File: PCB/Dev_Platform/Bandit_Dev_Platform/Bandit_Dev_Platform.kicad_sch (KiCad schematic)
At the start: 112 parts, among them J1 Conn_01x03_Pin, J10 Conn_01x05_Pin, J11 Conn_01x05_Pin, J2 SMA, J3 Conn_01x05_Pin, J4 Conn_01x05_Pin, J5 BNC, J6 BNC, J7 SMA, J8 Conn_01x05_Pin, J9 Conn_01x06_Pin, P1 USB_C_Plug_USB2.0, SW1 SW_SPST, U1 AD7253, U1 OPA1664, U2 RP2040, U3 AP2210N-4.0TRG1, U4 NCP164ASNADJT1G, U5 W25Q32JVSS, U6 MCP6486UT-E/OT, U7 MCP6S92-E/SN, Y1 12MHz

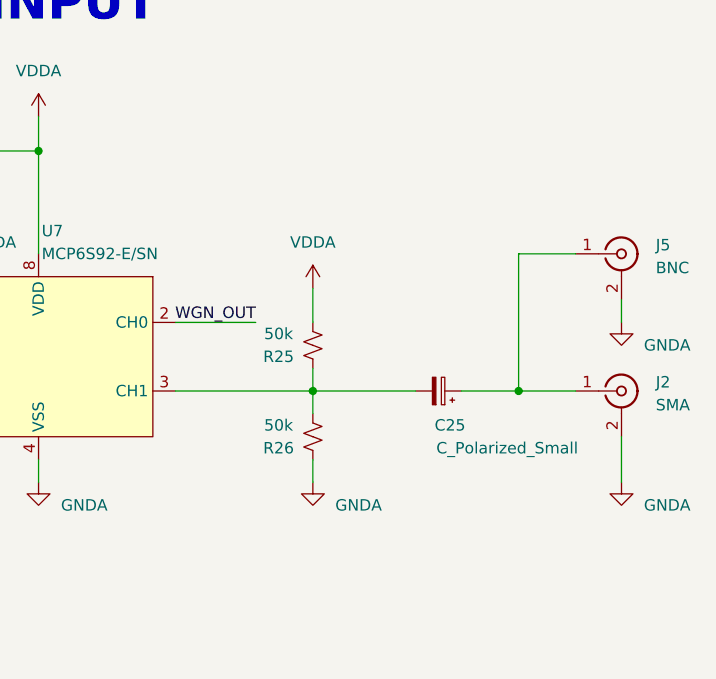
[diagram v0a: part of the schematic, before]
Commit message: update pcb, filter kinda done
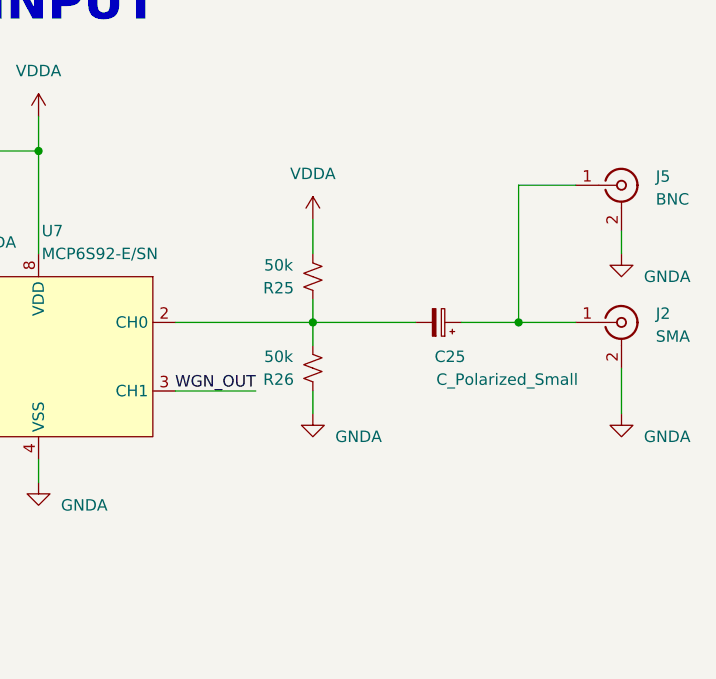
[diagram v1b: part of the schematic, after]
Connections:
- net WGN_OUT: now also U7.3 (CH1); no longer U7.2 (CH0)
- net at C25.2, R25.2, R26.1: now also U7.2 (CH0); no longer U7.3 (CH1)
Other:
- moved on the sheet: C25, J2, J5, R25, R26

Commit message: Josh said the tracks are great
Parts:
- added C17: 100n, Capacitor_SMD:C_0603_1608Metric, symbol Device:C_Small
- added C18: 10n, Capacitor_SMD:C_0603_1608Metric, symbol Device:C_Small
- added X1: SG-210STF, Oscillator:Oscillator_SMD_SeikoEpson_SG210-4Pin_2.5x2.0mm, symbol Oscillator:SG-210STF
- J5, J6: footprint (none) -> ADS8584SIPM:BNC_THT
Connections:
- net +3V3: now also C17.1, C18.1, X1.4 (Vcc)
- net GND: now also C17.2, C18.2, X1.2 (GND)
- net SE_SIG_A: now also R22.1; no longer R23.1
- net SE_SIG_B: now also R23.1; no longer R22.1
- net XIN renamed CLK_12M
- net CLK_12M: now also X1.3 (OUT)
- no-connect marks 4 -> 5

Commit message: Fixing dev pcb
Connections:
- net SE_SIG_A: now also U1.1, U1.2 (-); no longer U1.13 (-), U1.14
- net at C3.2, R3.2: now also U1.3 (+); no longer U1.10 (+)
- net at C4.1, R2.1: now also U1.1, U1.2 (-); no longer U1.8, U1.9 (-)
- net at C1.2, R1.2: now also U1.3 (+); no longer U1.12 (+)
- net at C5.2, R5.2: now also U1.10 (+); no longer U1.5 (+)
- net at C9.2, R7.2: now also U1.10 (+); no longer U1.3 (+)
- net at C3.2, R3.2: now also U1.12 (+); no longer U1.10 (+)
- net at C4.1, R2.1: now also U1.13 (-), U1.14; no longer U1.8, U1.9 (-)
- net at U1.6 (-), U1.7: now also R6.1; no longer C6.1, R4.1
- net at C9.2, R7.2: now also U1.5 (+); no longer U1.3 (+)
- new net: C6.1, R4.1, U1.8, U1.9 (-)
- new net: R6.1, U1.8, U1.9 (-)
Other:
- moved on the sheet: U1A, U1B, U1C, U1D
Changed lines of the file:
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@@
   (junction (at 259.08 382.27) (diameter 0) (color 0 0 0 0)
   )
+  (junction (at 367.03 295.91) (diameter 0) (color 0 0 0 0)
+  )
   (junction (at 334.01 254) (diameter 0) (color 0 0 0 0)
   )
@@
   (junction (at 191.77 349.25) (diameter 0) (color 0 0 0 0)
   )
-  (junction (at 318.77 294.64) (diameter 0) (color 0 0 0 0)
-  )
   (junction (at 505.46 57.15) (diameter 0) (color 0 0 0 0)
   )
   (junction (at 233.68 294.64) (diameter 0) (color 0 0 0 0)
   )
+  (junction (at 467.36 298.45) (diameter 0) (color 0 0 0 0)
+  )
   (junction (at 478.79 154.94) (diameter 0) (color 0 0 0 0)
   )
@@
   (junction (at 193.04 243.84) (diameter 0) (color 0 0 0 0)
   )
+  (junction (at 416.56 297.18) (diameter 0) (color 0 0 0 0)
+  )
   (junction (at 382.27 306.07) (diameter 0) (color 0 0 0 0)
   )
@@
   (junction (at 259.08 372.11) (diameter 0) (color 0 0 0 0)
   )
-  (junction (at 416.56 246.38) (diameter 0) (color 0 0 0 0)
-  )
   (junction (at 57.15 179.07) (diameter 0) (color 0 0 0 0)
   )
@@
   (junction (at 191.77 339.09) (diameter 0) (color 0 0 0 0)
   )
+  (junction (at 467.36 247.65) (diameter 0) (color 0 0 0 0)
+  )
   (junction (at 67.31 170.18) (diameter 0) (color 0 0 0 0)
   )
@@
   (junction (at 179.07 251.46) (diameter 0) (color 0 0 0 0)
   )
-  (junction (at 318.77 243.84) (diameter 0) (color 0 0 0 0)
-  )
   (junction (at 57.15 170.18) (diameter 0) (color 0 0 0 0)
   )
+  (junction (at 367.03 245.11) (diameter 0) (color 0 0 0 0)
+  )
   (junction (at 72.39 170.18) (diameter 0) (color 0 0 0 0)
   )
@@
   (junction (at 450.85 294.64) (diameter 0) (color 0 0 0 0)
   )
+  (junction (at 318.77 294.64) (diameter 0) (color 0 0 0 0)
+  )
   (junction (at 450.85 243.84) (diameter 0) (color 0 0 0 0)
   )
@@
   (junction (at 185.42 243.84) (diameter 0) (color 0 0 0 0)
   )
+  (junction (at 416.56 246.38) (diameter 0) (color 0 0 0 0)
+  )
   (junction (at 256.54 72.39) (diameter 0) (color 0 0 0 0)
   )
@@
   (junction (at 431.8 307.34) (diameter 0) (color 0 0 0 0)
   )
-  (junction (at 388.62 242.57) (diameter 0) (color 0 0 0 0)
-  )
-  (junction (at 467.36 247.65) (diameter 0) (color 0 0 0 0)
+  (junction (at 318.77 243.84) (diameter 0) (color 0 0 0 0)
   )
-  (junction (at 467.36 298.45) (diameter 0) (color 0 0 0 0)
+  (junction (at 388.62 242.57) (diameter 0) (color 0 0 0 0)
   )
   (junction (at 542.29 166.37) (diameter 0) (color 0 0 0 0)
@@
   (junction (at 53.34 340.36) (diameter 0) (color 0 0 0 0)
   )
-  (junction (at 367.03 245.11) (diameter 0) (color 0 0 0 0)
-  )
   (junction (at 209.55 77.47) (diameter 0) (color 0 0 0 0)
   )
   (junction (at 533.4 289.56) (diameter 0) (color 0 0 0 0)
   )
-  (junction (at 367.03 295.91) (diameter 0) (color 0 0 0 0)
-  )
   (junction (at 519.43 166.37) (diameter 0) (color 0 0 0 0)
   )
@@
   (junction (at 245.11 283.21) (diameter 0) (color 0 0 0 0)
   )
-  (junction (at 416.56 297.18) (diameter 0) (color 0 0 0 0)
-  )
   (junction (at 186.69 382.27) (diameter 0) (color 0 0 0 0)
   )
@@
     )
   )
-  (symbol (lib_id "Amplifier_Operational:TL074") (at 474.98 247.65 0) (mirror y) (unit 1)
+  (symbol (lib_id "Amplifier_Operational:TL074") (at 374.65 245.11 0) (mirror y) (unit 1)
     (in_bom yes) (on_board yes) (dnp no)
-    (property "Reference" "U1" (at 471.17 237.49 0)
+    (property "Reference" "U1" (at 370.84 234.95 0)
       (effects (font (size 1.27 1.27)))
     )
-    (property "Value" "OPA1664" (at 474.98 240.03 0)
+    (property "Value" "OPA1664" (at 374.65 237.49 0)
       (effects (font (size 1.27 1.27)))
     )
-    (property "Footprint" "Package_SO:SOIC-14_3.9x8.7mm_P1.27mm" (at 476.25 245.11 0)
+    (property "Footprint" "Package_SO:SOIC-14_3.9x8.7mm_P1.27mm" (at 375.92 242.57 0)
       (effects (font (size 1.27 1.27)) hide)
     )
-    (property "Datasheet" "http://www.ti.com/lit/ds/symlink/tl071.pdf" (at 473.71 242.57 0)
+    (property "Datasheet" "http://www.ti.com/lit/ds/symlink/tl071.pdf" (at 373.38 240.03 0)
       (effects (font (size 1.27 1.27)) hide)
     )
@@
     )
   )
-  (symbol (lib_id "Amplifier_Operational:TL074") (at 424.18 297.18 0) (mirror y) (unit 2)
+  (symbol (lib_id "Amplifier_Operational:TL074") (at 474.98 298.45 0) (mirror y) (unit 2)
     (in_bom yes) (on_board yes) (dnp no)
-    (property "Reference" "U1" (at 424.18 287.02 0)
+    (property "Reference" "U1" (at 474.98 288.29 0)
       (effects (font (size 1.27 1.27)))
     )
-    (property "Value" "OPA1664" (at 424.18 289.56 0)
+    (property "Value" "OPA1664" (at 474.98 290.83 0)
       (effects (font (size 1.27 1.27)))
     )
-    (property "Footprint" "Package_SO:SOIC-14_3.9x8.7mm_P1.27mm" (at 425.45 294.64 0)
+    (property "Footprint" "Package_SO:SOIC-14_3.9x8.7mm_P1.27mm" (at 476.25 295.91 0)
       (effects (font (size 1.27 1.27)) hide)
     )
-    (property "Datasheet" "http://www.ti.com/lit/ds/symlink/tl071.pdf" (at 422.91 292.1 0)
+    (property "Datasheet" "http://www.ti.com/lit/ds/symlink/tl071.pdf" (at 473.71 293.37 0)
       (effects (font (size 1.27 1.27)) hide)
     )
@@
     )
   )
-  (symbol (lib_id "Amplifier_Operational:TL074") (at 326.39 294.64 0) (mirror y) (unit 4)
+  (symbol (lib_id "Amplifier_Operational:TL074") (at 374.65 295.91 0) (mirror y) (unit 4)
     (in_bom yes) (on_board yes) (dnp no)
-    (property "Reference" "U1" (at 322.58 285.75 0)
+    (property "Reference" "U1" (at 370.84 287.02 0)
       (effects (font (size 1.27 1.27)))
     )
-    (property "Value" "OPA1664" (at 321.31 288.29 0)
+    (property "Value" "OPA1664" (at 369.57 289.56 0)
       (effects (font (size 1.27 1.27)))
     )
-    (property "Footprint" "Package_SO:SOIC-14_3.9x8.7mm_P1.27mm" (at 327.66 292.1 0)
+    (property "Footprint" "Package_SO:SOIC-14_3.9x8.7mm_P1.27mm" (at 375.92 293.37 0)
       (effects (font (size 1.27 1.27)) hide)
     )
-    (property "Datasheet" "http://www.ti.com/lit/ds/symlink/tl071.pdf" (at 325.12 289.56 0)
+    (property "Datasheet" "http://www.ti.com/lit/ds/symlink/tl071.pdf" (at 373.38 290.83 0)
       (effects (font (size 1.27 1.27)) hide)
     )
@@
     )
   )
-  (symbol (lib_id "Amplifier_Operational:TL074") (at 374.65 245.11 0) (mirror y) (unit 3)
+  (symbol (lib_id "Amplifier_Operational:TL074") (at 474.98 247.65 0) (mirror y) (unit 3)
     (in_bom yes) (on_board yes) (dnp no) (fields_autoplaced)
-    (property "Reference" "U1" (at 374.65 234.95 0)
+    (property "Reference" "U1" (at 474.98 237.49 0)
       (effects (font (size 1.27 1.27)))
     )
-    (property "Value" "OPA1664" (at 374.65 237.49 0)
+    (property "Value" "OPA1664" (at 474.98 240.03 0)
       (effects (font (size 1.27 1.27)))
     )
-    (property "Footprint" "Package_SO:SOIC-14_3.9x8.7mm_P1.27mm" (at 375.92 242.57 0)
+    (property "Footprint" "Package_SO:SOIC-14_3.9x8.7mm_P1.27mm" (at 476.25 245.11 0)
       (effects (font (size 1.27 1.27)) hide)
     )
-    (property "Datasheet" "http://www.ti.com/lit/ds/symlink/tl071.pdf" (at 373.38 240.03 0)
+    (property "Datasheet" "http://www.ti.com/lit/ds/symlink/tl071.pdf" (at 473.71 242.57 0)
       (effects (font (size 1.27 1.27)) hide)
     )
@@
     )
   )
-  (symbol (lib_id "Amplifier_Operational:TL074") (at 374.65 295.91 0) (mirror y) (unit 3)
+  (symbol (lib_id "Amplifier_Operational:TL074") (at 424.18 297.18 0) (mirror y) (unit 3)
     (in_bom yes) (on_board yes) (dnp no) (fields_autoplaced)
-    (property "Reference" "U1" (at 374.65 285.75 0)
+    (property "Reference" "U1" (at 424.18 287.02 0)
       (effects (font (size 1.27 1.27)))
     )
-    (property "Value" "OPA1664" (at 374.65 288.29 0)
+    (property "Value" "OPA1664" (at 424.18 289.56 0)
       (effects (font (size 1.27 1.27)))
     )
-    (property "Footprint" "Package_SO:SOIC-14_3.9x8.7mm_P1.27mm" (at 375.92 293.37 0)
+    (property "Footprint" "Package_SO:SOIC-14_3.9x8.7mm_P1.27mm" (at 425.45 294.64 0)
       (effects (font (size 1.27 1.27)) hide)
     )
-    (property "Datasheet" "http://www.ti.com/lit/ds/symlink/tl071.pdf" (at 373.38 290.83 0)
+    (property "Datasheet" "http://www.ti.com/lit/ds/symlink/tl071.pdf" (at 422.91 292.1 0)
       (effects (font (size 1.27 1.27)) hide)
     )
@@
     )
   )
-  (symbol (lib_id "Amplifier_Operational:TL074") (at 474.98 298.45 0) (mirror y) (unit 1)
+  (symbol (lib_id "Amplifier_Operational:TL074") (at 326.39 294.64 0) (mirror y) (unit 1)
     (in_bom yes) (on_board yes) (dnp no)
-    (property "Reference" "U1" (at 471.17 288.29 0)
+    (property "Reference" "U1" (at 322.58 284.48 0)
       (effects (font (size 1.27 1.27)))
     )
-    (property "Value" "OPA1664" (at 474.98 290.83 0)
+    (property "Value" "OPA1664" (at 326.39 287.02 0)
       (effects (font (size 1.27 1.27)))
     )
-    (property "Footprint" "Package_SO:SOIC-14_3.9x8.7mm_P1.27mm" (at 476.25 295.91 0)
+    (property "Footprint" "Package_SO:SOIC-14_3.9x8.7mm_P1.27mm" (at 327.66 292.1 0)
       (effects (font (size 1.27 1.27)) hide)
     )
-    (property "Datasheet" "http://www.ti.com/lit/ds/symlink/tl071.pdf" (at 473.71 293.37 0)
+    (property "Datasheet" "http://www.ti.com/lit/ds/symlink/tl071.pdf" (at 325.12 289.56 0)
       (effects (font (size 1.27 1.27)) hide)
     )

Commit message: PCB Fun
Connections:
- net SE_SIG_A: now also U1.8, U1.9 (-); no longer U1.1, U1.2 (-)
- net at C1.2, R1.2: now also U1.10 (+); no longer U1.3 (+)
- net at C5.2, R5.2: now also U1.3 (+); no longer U1.10 (+)
- net at C3.2, R3.2: now also U1.5 (+); no longer U1.12 (+)
- net at C4.1, R2.1: now also U1.6 (-), U1.7; no longer U1.13 (-), U1.14
- net at C9.2, R7.2: now also U1.12 (+); no longer U1.5 (+)
- net at C6.1, R4.1: now also U1.1, U1.2 (-); no longer U1.8, U1.9 (-)
- new net: R6.1, U1.13 (-), U1.14
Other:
- moved on the sheet: U1A, U1B, U1C, U1D
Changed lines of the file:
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@@
   (junction (at 259.08 382.27) (diameter 0) (color 0 0 0 0)
   )
-  (junction (at 367.03 295.91) (diameter 0) (color 0 0 0 0)
-  )
   (junction (at 334.01 254) (diameter 0) (color 0 0 0 0)
   )
@@
   (junction (at 233.68 294.64) (diameter 0) (color 0 0 0 0)
   )
-  (junction (at 467.36 298.45) (diameter 0) (color 0 0 0 0)
-  )
   (junction (at 478.79 154.94) (diameter 0) (color 0 0 0 0)
   )
@@
   (junction (at 193.04 243.84) (diameter 0) (color 0 0 0 0)
   )
-  (junction (at 416.56 297.18) (diameter 0) (color 0 0 0 0)
-  )
   (junction (at 382.27 306.07) (diameter 0) (color 0 0 0 0)
   )
@@
   (junction (at 519.43 64.77) (diameter 0) (color 0 0 0 0)
   )
+  (junction (at 416.56 297.18) (diameter 0) (color 0 0 0 0)
+  )
   (junction (at 179.07 243.84) (diameter 0) (color 0 0 0 0)
   )
@@
   (junction (at 438.15 243.84) (diameter 0) (color 0 0 0 0)
   )
+  (junction (at 318.77 294.64) (diameter 0) (color 0 0 0 0)
+  )
   (junction (at 186.69 349.25) (diameter 0) (color 0 0 0 0)
   )
   (junction (at 450.85 294.64) (diameter 0) (color 0 0 0 0)
   )
-  (junction (at 318.77 294.64) (diameter 0) (color 0 0 0 0)
+  (junction (at 467.36 298.45) (diameter 0) (color 0 0 0 0)
   )
   (junction (at 450.85 243.84) (diameter 0) (color 0 0 0 0)
   )
+  (junction (at 367.03 295.91) (diameter 0) (color 0 0 0 0)
+  )
   (junction (at 259.08 349.25) (diameter 0) (color 0 0 0 0)
   )
@@
     )
   )
-  (symbol (lib_id "Amplifier_Operational:TL074") (at 474.98 298.45 0) (mirror y) (unit 2)
+  (symbol (lib_id "Amplifier_Operational:TL074") (at 374.65 295.91 0) (mirror y) (unit 2)
     (in_bom yes) (on_board yes) (dnp no)
-    (property "Reference" "U1" (at 474.98 288.29 0)
+    (property "Reference" "U1" (at 374.65 285.75 0)
       (effects (font (size 1.27 1.27)))
     )
-    (property "Value" "OPA1664" (at 474.98 290.83 0)
+    (property "Value" "OPA1664" (at 374.65 288.29 0)
       (effects (font (size 1.27 1.27)))
     )
-    (property "Footprint" "Package_SO:SOIC-14_3.9x8.7mm_P1.27mm" (at 476.25 295.91 0)
+    (property "Footprint" "Package_SO:SOIC-14_3.9x8.7mm_P1.27mm" (at 375.92 293.37 0)
       (effects (font (size 1.27 1.27)) hide)
     )
-    (property "Datasheet" "http://www.ti.com/lit/ds/symlink/tl071.pdf" (at 473.71 293.37 0)
+    (property "Datasheet" "http://www.ti.com/lit/ds/symlink/tl071.pdf" (at 373.38 290.83 0)
       (effects (font (size 1.27 1.27)) hide)
     )
@@
     )
   )
-  (symbol (lib_id "Amplifier_Operational:TL074") (at 374.65 295.91 0) (mirror y) (unit 4)
+  (symbol (lib_id "Amplifier_Operational:TL074") (at 474.98 298.45 0) (mirror y) (unit 4)
     (in_bom yes) (on_board yes) (dnp no)
-    (property "Reference" "U1" (at 370.84 287.02 0)
+    (property "Reference" "U1" (at 471.17 289.56 0)
       (effects (font (size 1.27 1.27)))
     )
-    (property "Value" "OPA1664" (at 369.57 289.56 0)
+    (property "Value" "OPA1664" (at 469.9 292.1 0)
       (effects (font (size 1.27 1.27)))
     )
-    (property "Footprint" "Package_SO:SOIC-14_3.9x8.7mm_P1.27mm" (at 375.92 293.37 0)
+    (property "Footprint" "Package_SO:SOIC-14_3.9x8.7mm_P1.27mm" (at 476.25 295.91 0)
       (effects (font (size 1.27 1.27)) hide)
     )
-    (property "Datasheet" "http://www.ti.com/lit/ds/symlink/tl071.pdf" (at 373.38 290.83 0)
+    (property "Datasheet" "http://www.ti.com/lit/ds/symlink/tl071.pdf" (at 473.71 293.37 0)
       (effects (font (size 1.27 1.27)) hide)
     )
@@
     )
   )
-  (symbol (lib_id "Amplifier_Operational:TL074") (at 424.18 297.18 0) (mirror y) (unit 3)
+  (symbol (lib_id "Amplifier_Operational:TL074") (at 326.39 294.64 0) (mirror y) (unit 3)
     (in_bom yes) (on_board yes) (dnp no) (fields_autoplaced)
-    (property "Reference" "U1" (at 424.18 287.02 0)
+    (property "Reference" "U1" (at 326.39 284.48 0)
       (effects (font (size 1.27 1.27)))
     )
-    (property "Value" "OPA1664" (at 424.18 289.56 0)
+    (property "Value" "OPA1664" (at 326.39 287.02 0)
       (effects (font (size 1.27 1.27)))
     )
-    (property "Footprint" "Package_SO:SOIC-14_3.9x8.7mm_P1.27mm" (at 425.45 294.64 0)
+    (property "Footprint" "Package_SO:SOIC-14_3.9x8.7mm_P1.27mm" (at 327.66 292.1 0)
       (effects (font (size 1.27 1.27)) hide)
     )
-    (property "Datasheet" "http://www.ti.com/lit/ds/symlink/tl071.pdf" (at 422.91 292.1 0)
+    (property "Datasheet" "http://www.ti.com/lit/ds/symlink/tl071.pdf" (at 325.12 289.56 0)
       (effects (font (size 1.27 1.27)) hide)
     )
@@
     )
   )
-  (symbol (lib_id "Amplifier_Operational:TL074") (at 326.39 294.64 0) (mirror y) (unit 1)
+  (symbol (lib_id "Amplifier_Operational:TL074") (at 424.18 297.18 0) (mirror y) (unit 1)
     (in_bom yes) (on_board yes) (dnp no)
-    (property "Reference" "U1" (at 322.58 284.48 0)
+    (property "Reference" "U1" (at 420.37 287.02 0)
       (effects (font (size 1.27 1.27)))
     )
-    (property "Value" "OPA1664" (at 326.39 287.02 0)
+    (property "Value" "OPA1664" (at 424.18 289.56 0)
       (effects (font (size 1.27 1.27)))
     )
-    (property "Footprint" "Package_SO:SOIC-14_3.9x8.7mm_P1.27mm" (at 327.66 292.1 0)
+    (property "Footprint" "Package_SO:SOIC-14_3.9x8.7mm_P1.27mm" (at 425.45 294.64 0)
       (effects (font (size 1.27 1.27)) hide)
     )
-    (property "Datasheet" "http://www.ti.com/lit/ds/symlink/tl071.pdf" (at 325.12 289.56 0)
+    (property "Datasheet" "http://www.ti.com/lit/ds/symlink/tl071.pdf" (at 422.91 292.1 0)
       (effects (font (size 1.27 1.27)) hide)
     )

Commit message: PCB Update
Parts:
- C23, C24: value 36n C0G -> 16n C0G
- R21, R22, R23, R24: value 10R -> 20R
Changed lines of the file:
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@@
       (effects (font (size 1.27 1.27)))
     )
-    (property "Value" "10R" (at 247.65 295.91 90)
+    (property "Value" "20R" (at 247.65 295.91 90)
       (effects (font (size 1.27 1.27)))
     )
@@
       (effects (font (size 1.27 1.27)) (justify left))
     )
-    (property "Value" "36n C0G" (at 247.65 288.2963 0)
+    (property "Value" "16n C0G" (at 247.65 288.2963 0)
       (effects (font (size 1.27 1.27)) (justify left))
     )
@@
       (effects (font (size 1.27 1.27)) (justify left))
     )
-    (property "Value" "36n C0G" (at 247.65 270.5163 0)
+    (property "Value" "16n C0G" (at 247.65 270.5163 0)
       (effects (font (size 1.27 1.27)) (justify left))
     )
@@
       (effects (font (size 1.27 1.27)))
     )
-    (property "Value" "10R" (at 251.46 261.62 90)
+    (property "Value" "20R" (at 251.46 261.62 90)
       (effects (font (size 1.27 1.27)))
     )
@@
       (effects (font (size 1.27 1.27)))
     )
-    (property "Value" "10R" (at 247.65 276.86 90)
+    (property "Value" "20R" (at 247.65 276.86 90)
       (effects (font (size 1.27 1.27)))
     )
@@
       (effects (font (size 1.27 1.27)))
     )
-    (property "Value" "10R" (at 247.65 280.67 90)
-      (effects (font (size 1.27 1.27)))
-    )
+    (property "Value" "20R" (at 247.65 280.67 90)
+      (effects (font (size 1.27 1.27)))
+    )
